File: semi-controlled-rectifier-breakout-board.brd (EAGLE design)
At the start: 118.1 x 165.1 mm, 16 parts, among them U10 VO3053-X007T, U11 VO3053-X007T, U8 TN4015H-6G, U9 TN4015H-6G, X1 22-23-2031

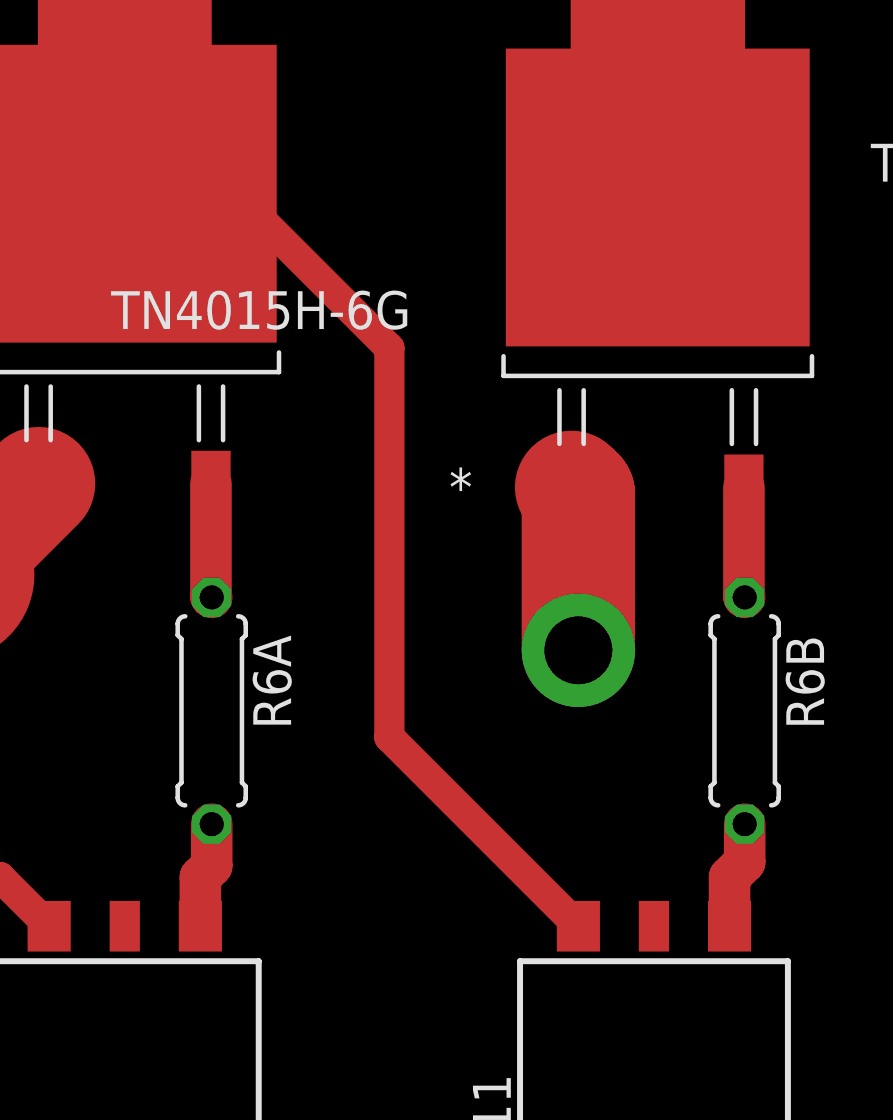
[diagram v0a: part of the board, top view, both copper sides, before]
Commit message: Modified flatcam files and brd layout
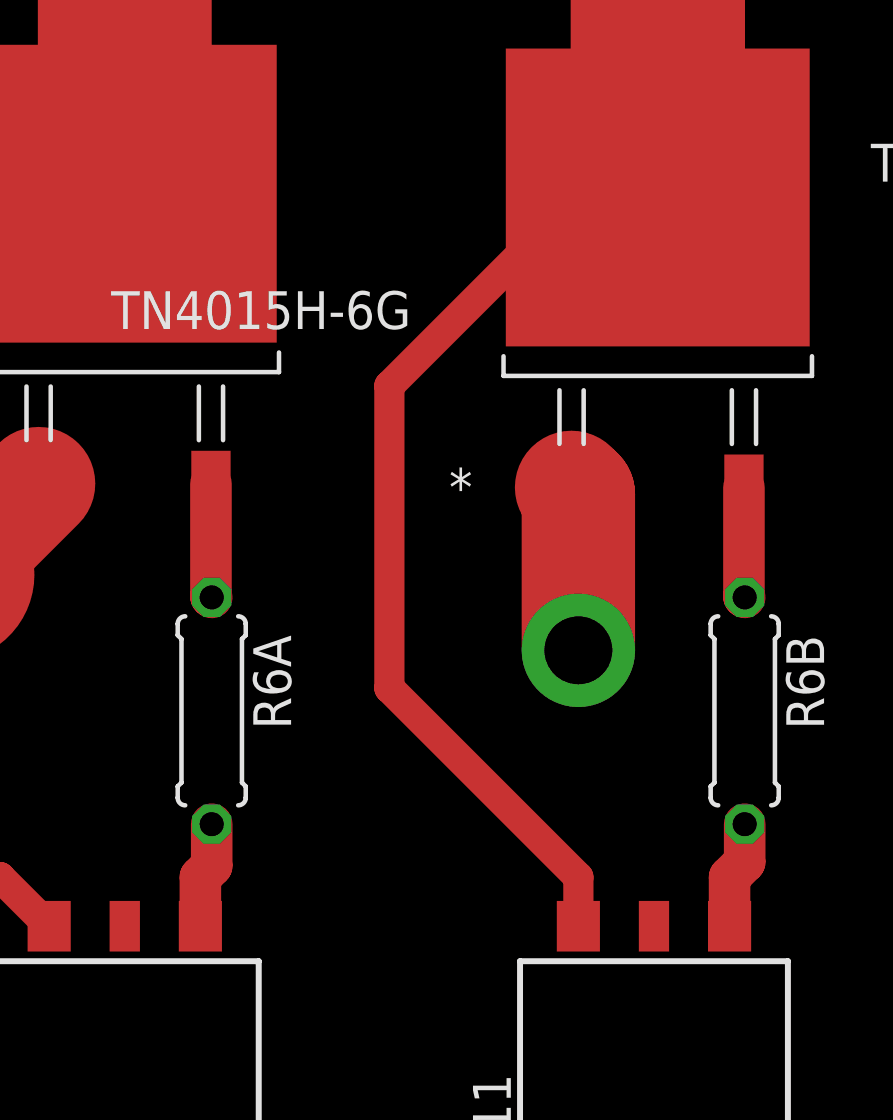
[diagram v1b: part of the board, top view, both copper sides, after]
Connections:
- net P1_FUSED: no longer U11.6
- net P2_IN: now also U11.6
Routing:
- net P2_IN: track 39.4 -> 71.8 mm
- net P1_FUSED: track 111.0 -> 81.6 mm
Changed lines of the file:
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@@
 <wire x1="43.18" y1="128.1684" x2="43.307" y2="128.0414" width="5.842" layer="1"/>
 <wire x1="43.307" y1="128.0414" x2="43.307" y2="111.7346" width="5.842" layer="1"/>
+<contactref element="U11" pad="6"/>
+<wire x1="43.307" y1="111.7346" x2="40.6146" y2="111.7346" width="1.016" layer="1"/>
+<wire x1="34.29" y1="95.25" x2="40.64" y2="88.9" width="1.016" layer="1"/>
+<wire x1="40.64" y1="88.9" x2="40.64" y2="87.25" width="1.016" layer="1"/>
+<wire x1="40.6146" y1="111.7346" x2="34.29" y2="105.41" width="1.016" layer="1"/>
+<wire x1="34.29" y1="105.41" x2="34.29" y2="95.25" width="1.016" layer="1"/>
 </signal>
 <signal name="P1_FUSED">
 <contactref element="U8" pad="3"/>
 <contactref element="D8" pad="3"/>
-<contactref element="U11" pad="6"/>
 <contactref element="U10" pad="6"/>
 <wire x1="25.4" y1="111.8616" x2="25.4" y2="128.1684" width="5.842" layer="1"/>
 <contactref element="U$1" pad="1"/>
 <wire x1="25.4" y1="128.1684" x2="12.7" y2="128.1684" width="5.842" layer="1"/>
-<wire x1="40.64" y1="87.25" x2="34.29" y2="93.6" width="1.016" layer="1"/>
-<wire x1="34.29" y1="106.68" x2="34.29" y2="93.6" width="1.016" layer="1"/>
 <wire x1="25.4" y1="111.8616" x2="29.1084" y2="111.8616" width="1.016" layer="1"/>
-<wire x1="29.1084" y1="111.8616" x2="34.29" y2="106.68" width="1.016" layer="1"/>
 <wire x1="22.86" y1="87.25" x2="21.21" y2="88.9" width="1.016" layer="1"/>
 <wire x1="21.21" y1="88.9" x2="11.43" y2="88.9" width="1.016" layer="1"/>

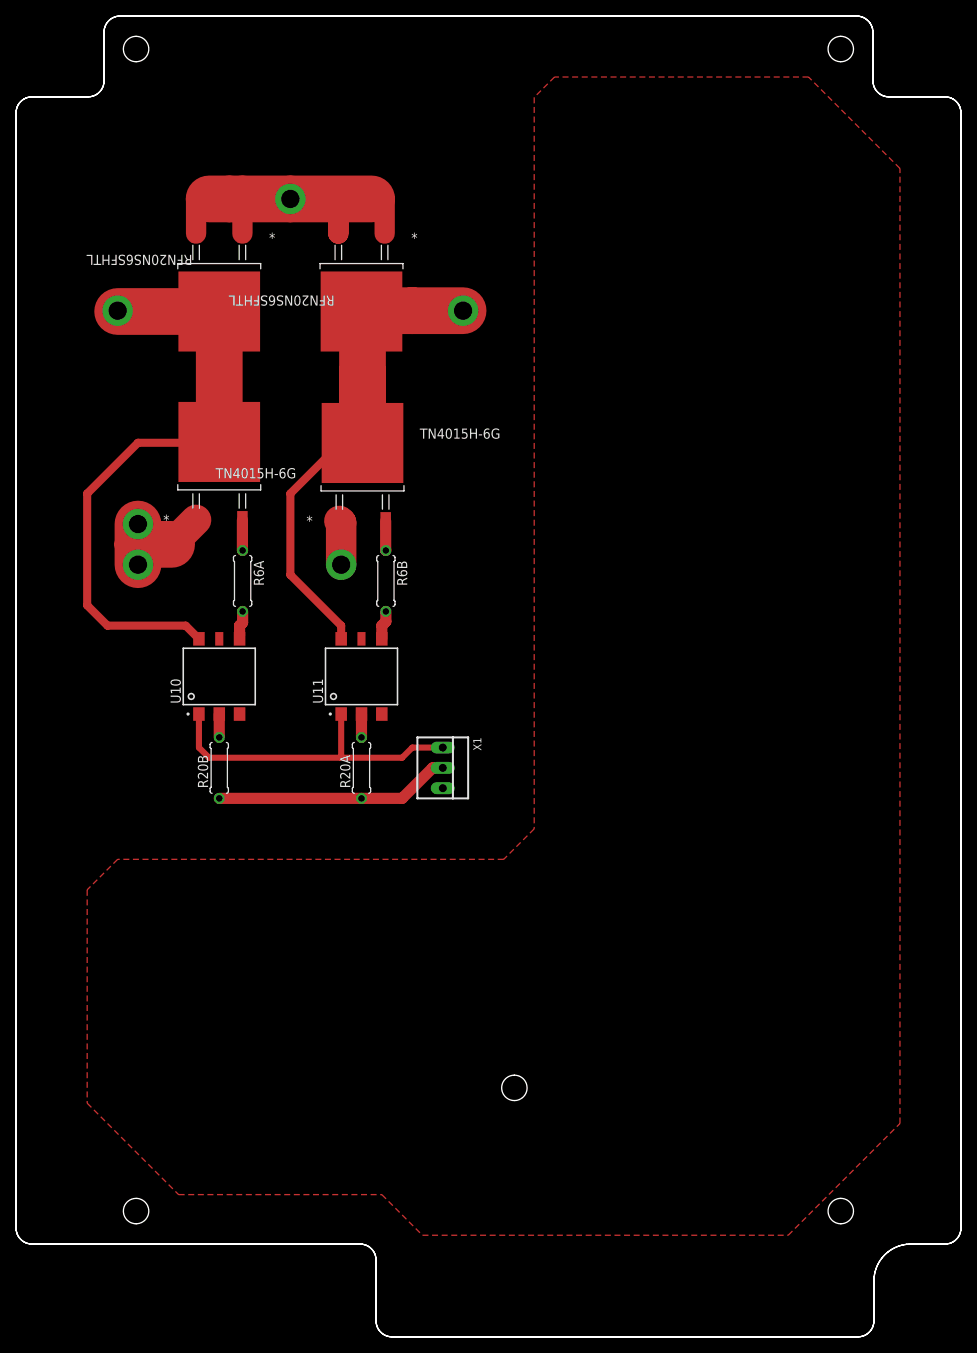
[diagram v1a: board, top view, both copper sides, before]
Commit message: Created new cam file, started new flatcam project, and added silkscreen layer for labeling
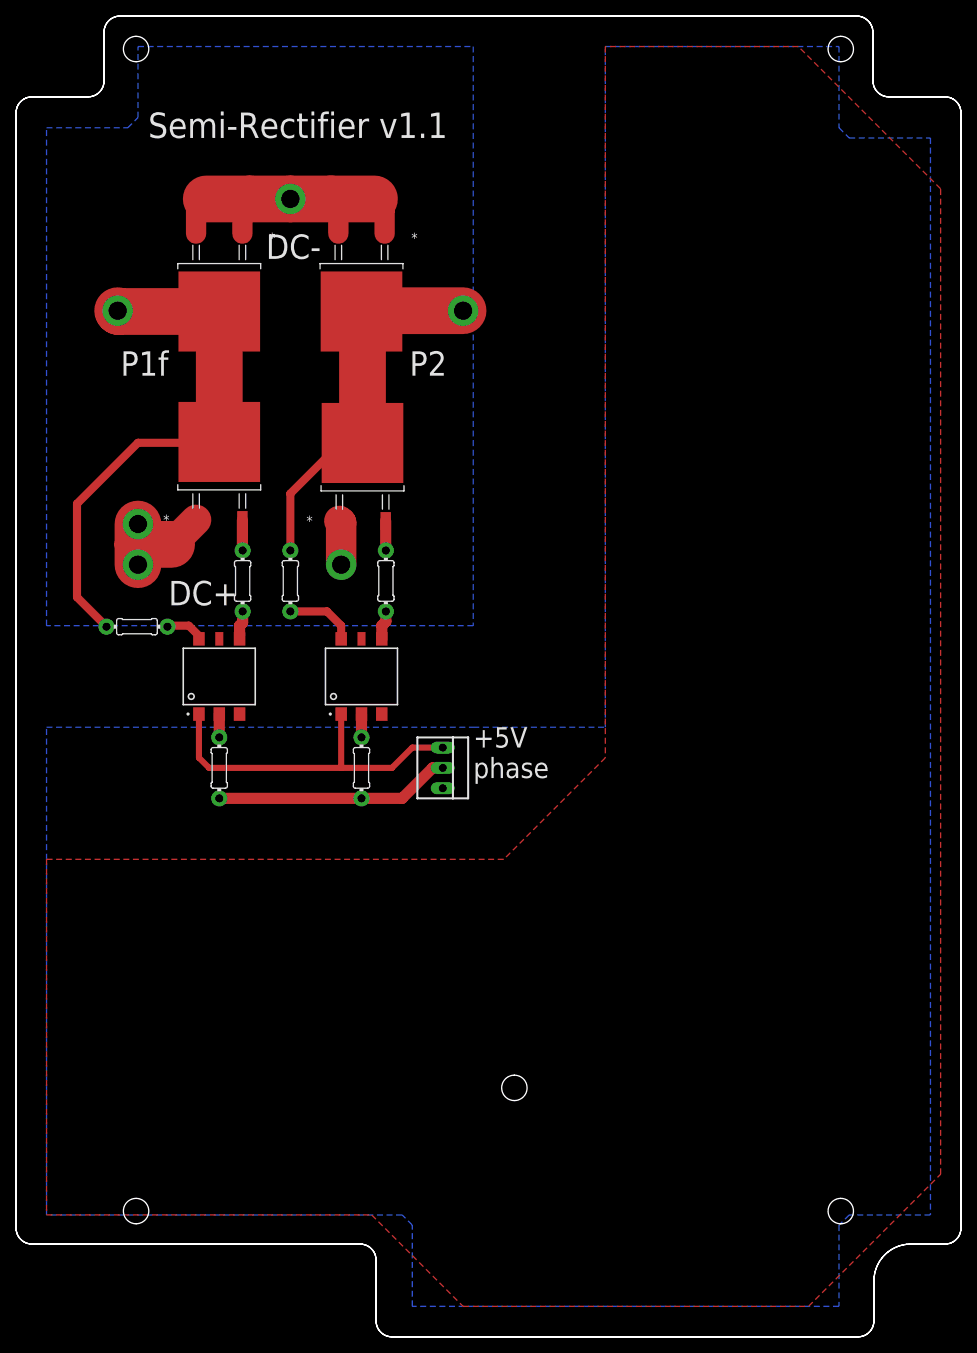
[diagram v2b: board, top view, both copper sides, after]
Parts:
- added D1, D2: DIODE, RectifierParts:0204/7_TH
- R20A, R20B: value (none) -> 200; device rcl:0207/7 -> RectifierParts:0204/7_TH
- R6A, R6B: value (none) -> 180; device rcl:0207/7 -> RectifierParts:0204/7_TH
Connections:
- new net N$3: D1.P$2, U11.6
- new net N$9: D2.P$2, U10.6
- net N$2: now also R6A.P$2; no longer R6A.2
- net N$4: now also R6B.P$2; no longer R6B.2
- net N$5: now also R6A.P$1; no longer R6A.1
- net N$6: now also R6B.P$1; no longer R6B.1
- net N$7: now also R20A.P$2; no longer R20A.2
- net N$8: now also R20B.P$2; no longer R20B.2
- net P1_FUSED: now also D2.P$1; no longer U10.6
- net P2_IN: now also D1.P$1; no longer U11.6
- net PHASE_CONTROL_SIGNAL: now also R20A.P$1, R20B.P$1; no longer R20A.1, R20B.1
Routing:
- net P2_IN: track 71.8 -> 48.0 mm
- net P1_FUSED: track 81.6 -> 72.0 mm
- net N$3: track 0.00 -> 8.74 mm
- net DC-: track 48.6 -> 40.2 mm
- net N$9: track 0.00 -> 4.90 mm
- net +5VDC: track 41.2 -> 44.2 mm
- added copper zone on layer 16, net AC_BACK
- added copper zone on layer 16, net DC_BACK
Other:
- board text added: "+5V"
- board text added: "DC+"
- board text added: "DC-"
- board text added: "P1f"
- board text added: "P2"
- board text added: "Semi-Rectifier v1.1"
- board text added: "phase"

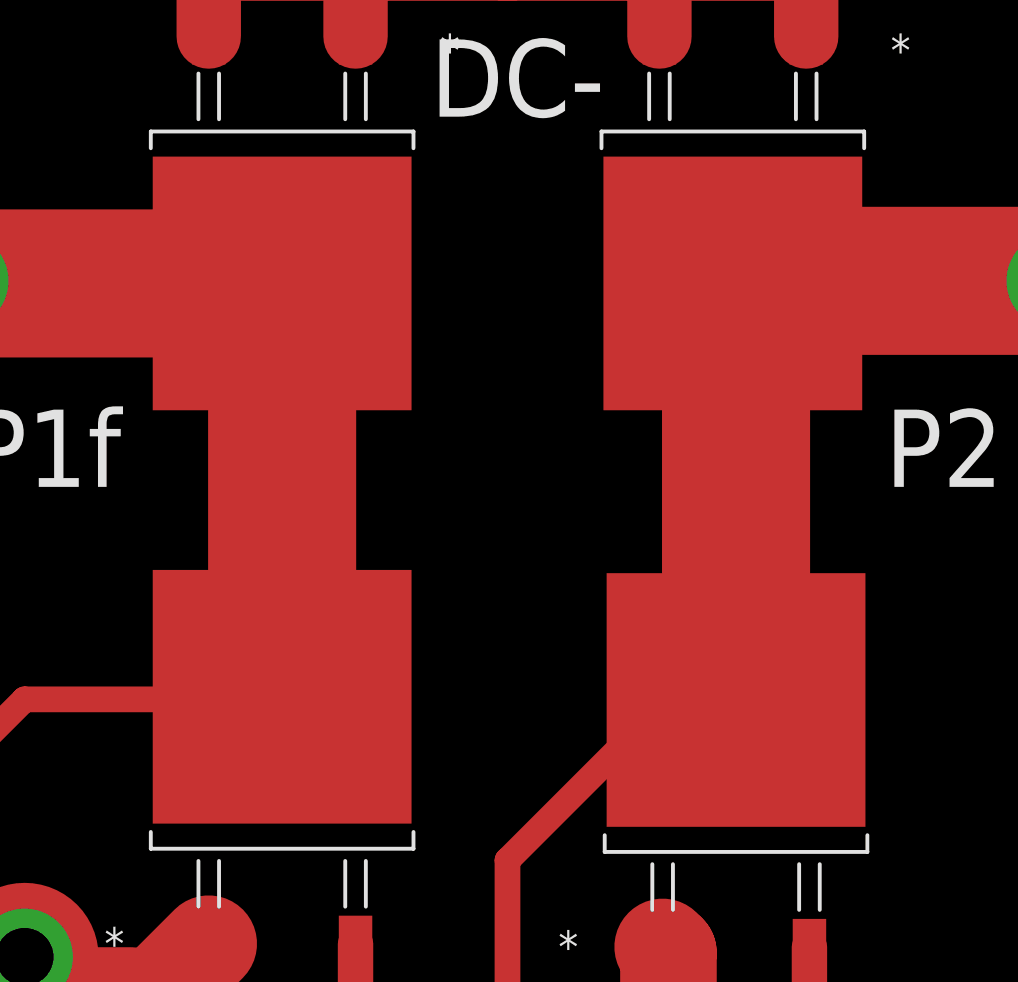
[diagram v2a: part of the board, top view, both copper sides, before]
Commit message: Increased P1,P2 trace width on board and added thermal vias. Exported CAM file and worked on flatcam project
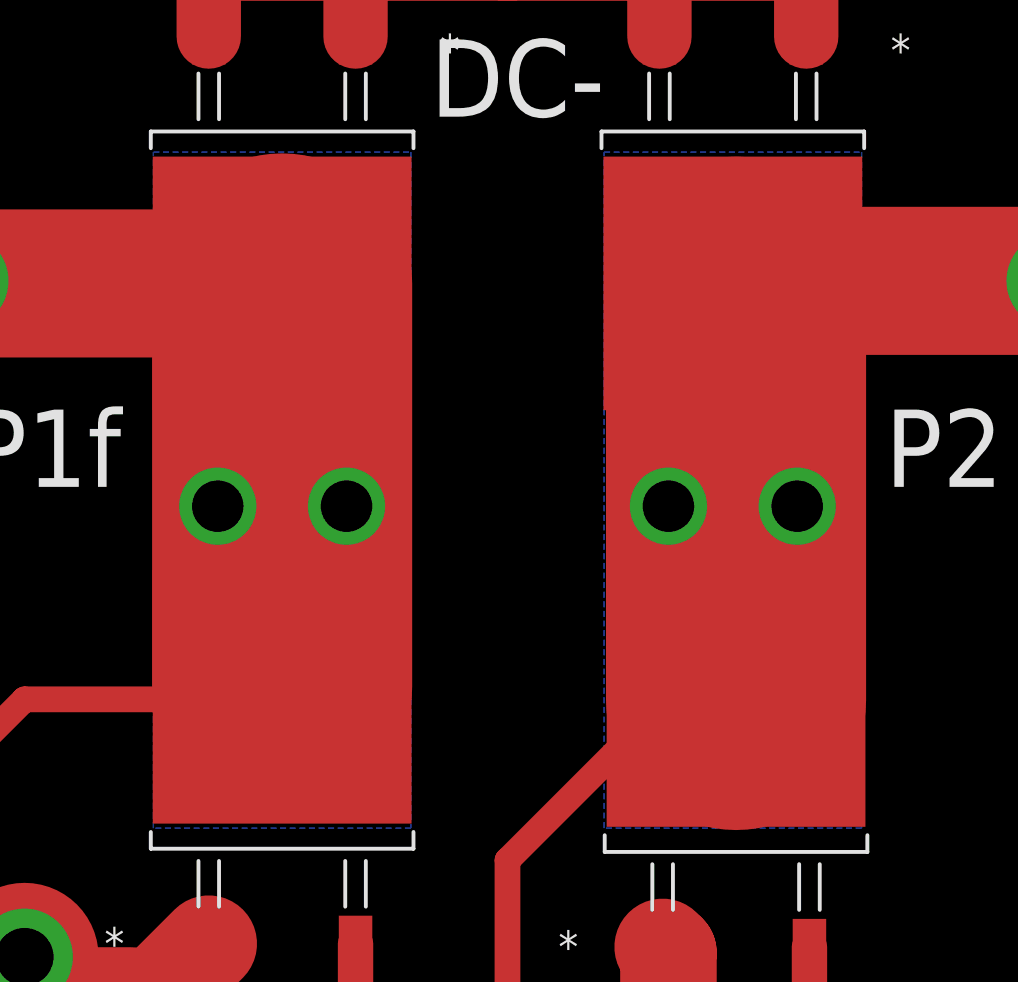
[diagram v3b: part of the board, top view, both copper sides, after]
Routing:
- net P1_FUSED: track 72.0 -> 70.2 mm, vias 0 -> 2
- net P2_IN: vias 0 -> 2
- added copper zone on layer 16, net P1_FUSED
- added copper zone on layer 16, net P2_IN
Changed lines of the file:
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@@
 <contactref element="U$2" pad="1"/>
 <wire x1="43.18" y1="128.1684" x2="43.307" y2="128.0414" width="5.842" layer="1"/>
-<wire x1="43.307" y1="128.0414" x2="43.307" y2="111.7346" width="5.842" layer="1"/>
+<wire x1="43.307" y1="128.0414" x2="43.307" y2="111.7346" width="10.2616" layer="1"/>
 <wire x1="43.307" y1="111.7346" x2="40.6146" y2="111.7346" width="1.016" layer="1"/>
 <wire x1="40.6146" y1="111.7346" x2="34.29" y2="105.41" width="1.016" layer="1"/>
@@
 <wire x1="43.18" y1="128.1684" x2="43.2816" y2="128.27" width="5.842" layer="1"/>
 <wire x1="43.2816" y1="128.27" x2="55.88" y2="128.27" width="5.842" layer="1"/>
+<polygon width="0.127" layer="16">
+<vertex x="38.1" y="133.35"/>
+<vertex x="48.26" y="133.35"/>
+<vertex x="48.26" y="106.68"/>
+<vertex x="38.1" y="106.68"/>
+</polygon>
+<via x="40.64" y="119.38" extent="1-16" drill="2.032"/>
+<via x="45.72" y="119.38" extent="1-16" drill="2.032"/>
+<wire x1="45.72" y1="119.38" x2="43.307" y2="111.7346" width="0" layer="19" extent="1-1"/>
 </signal>
 <signal name="P1_FUSED">
@@
 <wire x1="25.4" y1="128.1684" x2="12.8016" y2="128.1684" width="5.842" layer="1"/>
 <wire x1="12.8016" y1="128.1684" x2="12.7" y2="128.27" width="5.842" layer="1"/>
-<wire x1="25.4" y1="128.1684" x2="25.4" y2="110.49" width="5.842" layer="1"/>
-<wire x1="25.4" y1="111.8616" x2="25.4" y2="110.49" width="0" layer="19" extent="1-1"/>
+<wire x1="25.4" y1="128.1684" x2="25.4" y2="112.268" width="10.2616" layer="1"/>
+<polygon width="0.127" layer="16" isolate="1.27">
+<vertex x="20.32" y="133.35"/>
+<vertex x="30.48" y="133.35"/>
+<vertex x="30.48" y="106.68"/>
+<vertex x="20.32" y="106.68"/>
+</polygon>
+<via x="27.94" y="119.38" extent="1-16" drill="2.032"/>
+<via x="22.86" y="119.38" extent="1-16" drill="2.032"/>
+<wire x1="25.4" y1="111.8616" x2="25.4" y2="112.268" width="0" layer="19" extent="1-1"/>
+<wire x1="22.86" y1="119.38" x2="25.4" y2="112.268" width="0" layer="19" extent="1-1"/>
 </signal>
 <signal name="DC+">
@@
 </signal>
 <signal name="AC_BACK">
-<polygon width="2.54" layer="16" isolate="2.54" thermals="no">
+<polygon width="2.54" layer="16" isolate="2.54" thermals="no" rank="2">
 <vertex x="3.81" y="151.13"/>
 <vertex x="13.97" y="151.13"/>
